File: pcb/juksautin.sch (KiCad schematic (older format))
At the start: 26 parts, among them J1 Screw_Terminal_01x09, J3 AVR-ISP-6, J4 Conn_01x09, U1 SP3485EN, U2 SRV05-4, U3 R-78E5.0-0.5, U4 ATmega328P-AU, Y1 X322516MLB4SI

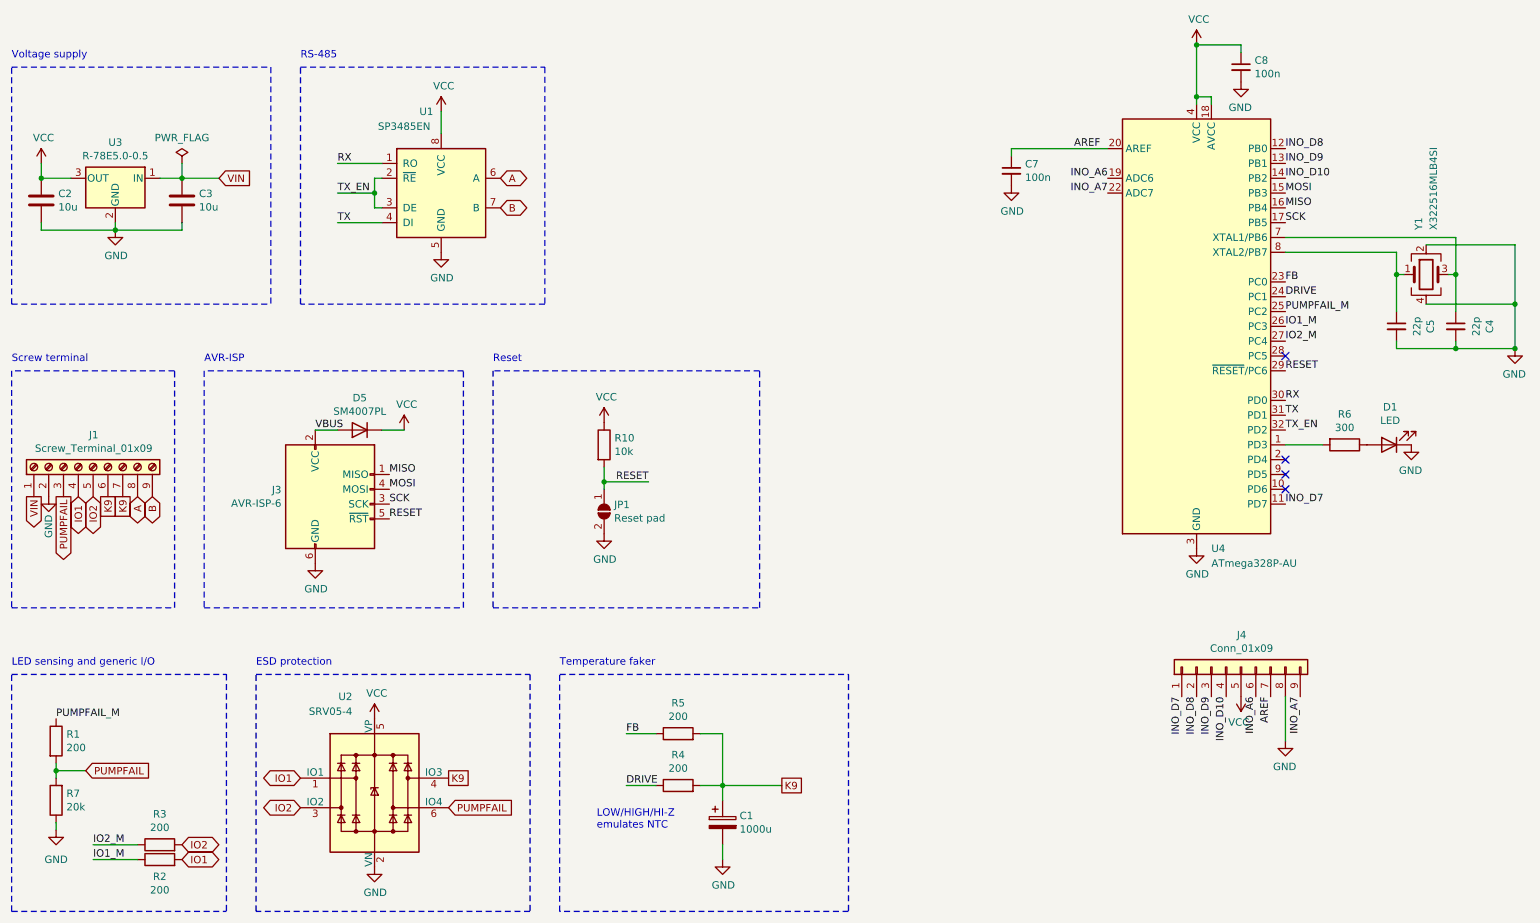
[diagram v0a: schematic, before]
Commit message: pcb: Add debug header for serial comm, reduce unique capacitor count by 1
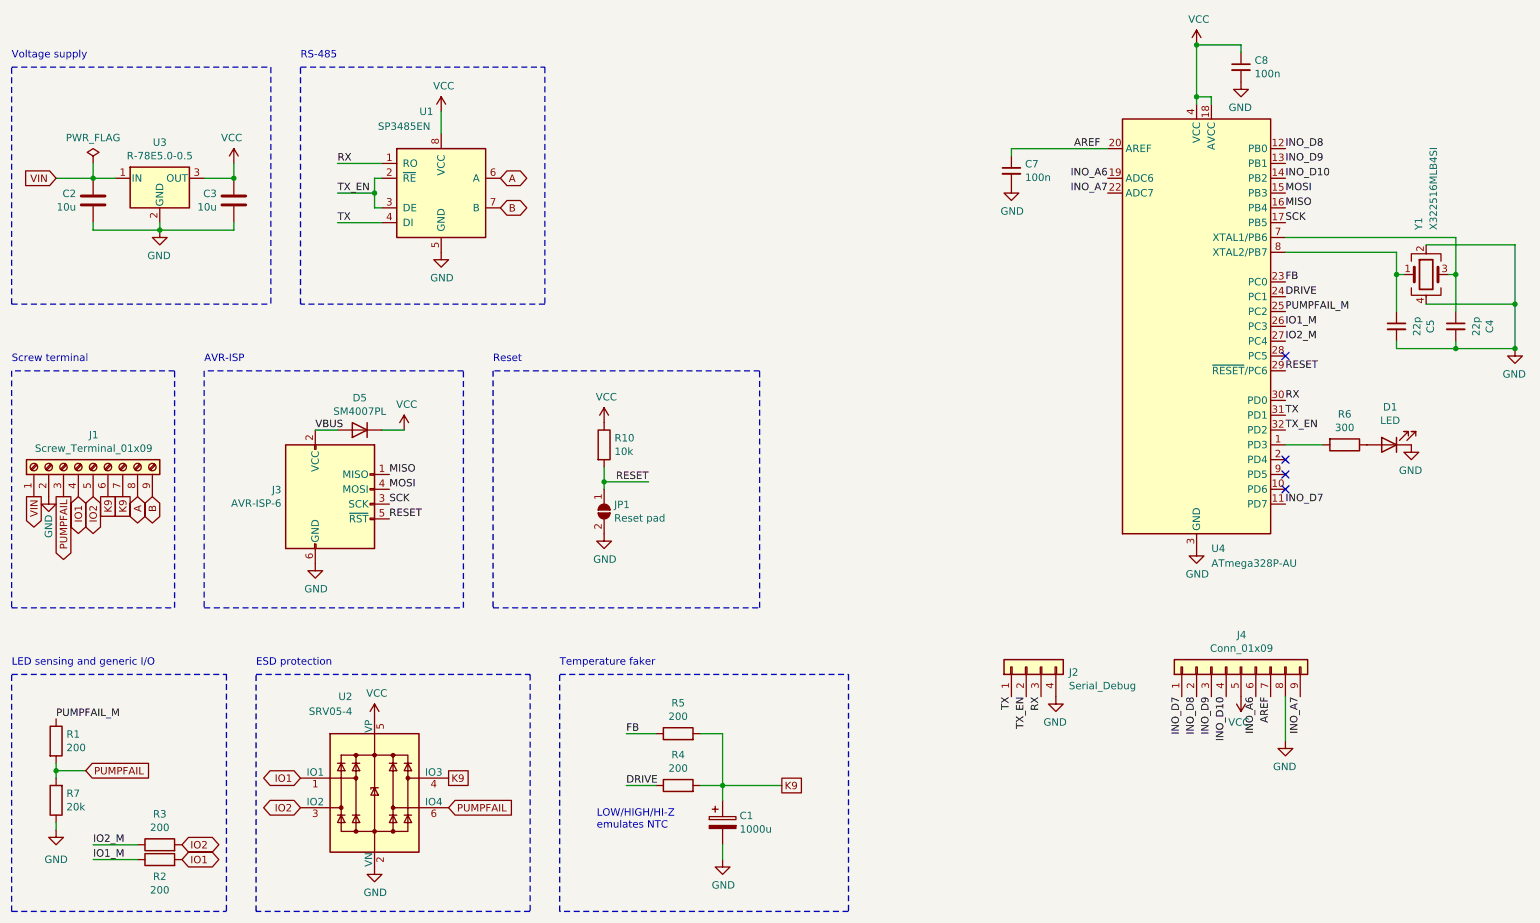
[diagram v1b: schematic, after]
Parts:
- removed C2: 10u, Capacitor_SMD:C_0402_1005Metric, symbol Device:C
- added C3: 10u, Capacitor_SMD:C_1206_3216Metric, symbol Device:C
- added J2: Serial_Debug, Connector_PinHeader_1.27mm:PinHeader_1x04_P1.27mm_Vertical, symbol Connector_Generic:Conn_01x04
- renumbered C3 to C2
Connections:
- net GND: now also C3.2, J2.4 (Pin_4)
- net RX: now also J2.3 (Pin_3)
- net TX: now also J2.1 (Pin_1)
- net TX_EN: now also J2.2 (Pin_2)
- net VCC: now also C3.1
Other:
- moved on the sheet: C2, U3
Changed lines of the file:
@@
 L power:GND #PWR0109
 U 1 1 60C41985
-P 1550 2100
-F 0 "#PWR0109" H 1550 1850 50  0001 C CNN
-F 1 "GND" H 1555 1927 50  0000 C CNN
-F 2 "" H 1550 2100 50  0001 C CNN
-F 3 "" H 1550 2100 50  0001 C CNN
-	1    1550 2100
-	1    0    0    -1
-$EndComp
-Text GLabel 2250 1750 2    50   Input ~ 0
+P 1850 2100
+F 0 "#PWR0109" H 1850 1850 50  0001 C CNN
+F 1 "GND" H 1855 1927 50  0000 C CNN
+F 2 "" H 1850 2100 50  0001 C CNN
+F 3 "" H 1850 2100 50  0001 C CNN
+	1    1850 2100
+	-1   0    0    -1
+$EndComp
+Text GLabel 1150 1750 0    50   Input ~ 0
 VIN
 $Comp
 L power:PWR_FLAG #FLG0101
 U 1 1 60C4198C
-P 2000 1650
-F 0 "#FLG0101" H 2000 1725 50  0001 C CNN
-F 1 "PWR_FLAG" H 2000 1823 50  0000 C CNN
-F 2 "" H 2000 1650 50  0001 C CNN
-F 3 "~" H 2000 1650 50  0001 C CNN
-	1    2000 1650
-	1    0    0    -1
+P 1400 1650
+F 0 "#FLG0101" H 1400 1725 50  0001 C CNN
+F 1 "PWR_FLAG" H 1400 1823 50  0000 C CNN
+F 2 "" H 1400 1650 50  0001 C CNN
+F 3 "~" H 1400 1650 50  0001 C CNN
+	1    1400 1650
+	-1   0    0    -1
 $EndComp
 $Comp
 L Regulator_Switching:R-78E5.0-0.5 U3
 U 1 1 60C41992
-P 1550 1750
-F 0 "U3" H 1550 1992 50  0000 C CNN
-F 1 "R-78E5.0-0.5" H 1550 1901 50  0000 C CNN
-F 2 "Converter_DCDC:Converter_DCDC_RECOM_R-78E-0.5_THT" H 1600 1500 50  0001 L CIN
-F 3 "https://www.recom-power.com/pdf/Innoline/R-78Exx-0.5.pdf" H 1550 1750 50  0001 C CNN
-	1    1550 1750
-	-1   0    0    -1
-$EndComp
-Wire Wire Line
-	1850 1750 2000 1750
-Wire Wire Line
-	2000 1650 2000 1750
-Connection ~ 2000 1750
-Wire Wire Line
-	2000 1750 2250 1750
-Wire Wire Line
-	1550 2050 1550 2100
-Connection ~ 1550 2100
-Wire Wire Line
-	2000 2050 2000 2100
-Wire Wire Line
-	2000 2100 1550 2100
+P 1850 1750
+F 0 "U3" H 1850 1992 50  0000 C CNN
+F 1 "R-78E5.0-0.5" H 1850 1901 50  0000 C CNN
+F 2 "Converter_DCDC:Converter_DCDC_RECOM_R-78E-0.5_THT" H 1900 1500 50  0001 L CIN
+F 3 "https://www.recom-power.com/pdf/Innoline/R-78Exx-0.5.pdf" H 1850 1750 50  0001 C CNN
+	1    1850 1750
+	1    0    0    -1
+$EndComp
+Wire Wire Line
+	1550 1750 1400 1750
+Wire Wire Line
+	1400 1650 1400 1750
+Connection ~ 1400 1750
+Wire Wire Line
+	1400 1750 1150 1750
+Wire Wire Line
+	1850 2050 1850 2100
+Connection ~ 1850 2100
+Wire Wire Line
+	1400 2050 1400 2100
+Wire Wire Line
+	1400 2100 1850 2100
 $Comp
 L power:VCC #PWR0111
 U 1 1 60C419A0
-P 1050 1650
-F 0 "#PWR0111" H 1050 1500 50  0001 C CNN
-F 1 "VCC" H 1065 1823 50  0000 C CNN
-F 2 "" H 1050 1650 50  0001 C CNN
-F 3 "" H 1050 1650 50  0001 C CNN
-	1    1050 1650
-	1    0    0    -1
-$EndComp
-Wire Wire Line
-	1250 1750 1050 1750
+P 2350 1650
+F 0 "#PWR0111" H 2350 1500 50  0001 C CNN
+F 1 "VCC" H 2365 1823 50  0000 C CNN
+F 2 "" H 2350 1650 50  0001 C CNN
+F 3 "" H 2350 1650 50  0001 C CNN
+	1    2350 1650
+	-1   0    0    -1
+$EndComp
+Wire Wire Line
+	2150 1750 2350 1750
 Wire Notes Line
 	850  1000 2600 1000
@@
 Text Notes 850  950  0    50   ~ 0
 Voltage supply
-$Comp
-L Device:C C2
-U 1 1 60C419AC
-P 1050 1900
-F 0 "C2" H 1165 1946 50  0000 L CNN
-F 1 "10u" H 1165 1855 50  0000 L CNN
-F 2 "Capacitor_SMD:C_0402_1005Metric" H 1088 1750 50  0001 C CNN
-F 3 "~" H 1050 1900 50  0001 C CNN
-F 4 "C15525" H 1050 1900 50  0001 C CNN "LCSC"
-	1    1050 1900
-	1    0    0    -1
-$EndComp
-$Comp
-L Device:C C3
-U 1 1 60C419B2
-P 2000 1900
-F 0 "C3" H 2115 1946 50  0000 L CNN
-F 1 "10u" H 2115 1855 50  0000 L CNN
-F 2 "Capacitor_SMD:C_1206_3216Metric" H 2038 1750 50  0001 C CNN
-F 3 "~" H 2000 1900 50  0001 C CNN
-F 4 "C13585" H 2000 1900 50  0001 C CNN "LCSC"
-	1    2000 1900
-	1    0    0    -1
-$EndComp
-Connection ~ 1050 1750
-Wire Wire Line
-	1550 2100 1050 2100
-Wire Wire Line
-	1050 2100 1050 2050
-Wire Wire Line
-	1050 1650 1050 1750
+Wire Wire Line
+	1850 2100 2350 2100
+Wire Wire Line
+	2350 2100 2350 2050
+Wire Wire Line
+	2350 1650 2350 1750
 Wire Notes Line
 	850  2600 2600 2600
@@
 Wire Wire Line
 	10600 2900 10200 2900
+Text Label 7800 5250 3    50   ~ 0
+RX
+Text Label 7600 5250 3    50   ~ 0
+TX
+Text Label 7700 5250 3    50   ~ 0
+TX_EN
+$Comp
+L power:GND #PWR0110
+U 1 1 60D1EC45
+P 7900 5250
+F 0 "#PWR0110" H 7900 5000 50  0001 C CNN
+F 1 "GND" H 7905 5077 50  0000 C CNN
+F 2 "" H 7900 5250 50  0001 C CNN
+F 3 "" H 7900 5250 50  0001 C CNN
+	1    7900 5250
+	-1   0    0    -1
+$EndComp
+$Comp
+L Connector_Generic:Conn_01x04 J2
+U 1 1 60D1A962
+P 7700 5050
+F 0 "J2" V 7664 4762 50  0000 R CNN
+F 1 "Serial_Debug" V 7573 4762 50  0000 R CNN
+F 2 "Connector_PinHeader_1.27mm:PinHeader_1x04_P1.27mm_Vertical" H 7700 5050 50  0001 C CNN
+F 3 "~" H 7700 5050 50  0001 C CNN
+	1    7700 5050
+	0    -1   -1   0
+$EndComp
+$Comp
+L Device:C C2
+U 1 1 60C419B2
+P 1400 1900
+F 0 "C2" H 1515 1946 50  0000 L CNN
+F 1 "10u" H 1515 1855 50  0000 L CNN
+F 2 "Capacitor_SMD:C_1206_3216Metric" H 1438 1750 50  0001 C CNN
+F 3 "~" H 1400 1900 50  0001 C CNN
+F 4 "C13585" H 1400 1900 50  0001 C CNN "LCSC"
+	1    1400 1900
+	-1   0    0    -1
+$EndComp
+$Comp
+L Device:C C3
+U 1 1 60D40841
+P 2350 1900
+F 0 "C3" H 2465 1946 50  0000 L CNN
+F 1 "10u" H 2465 1855 50  0000 L CNN
+F 2 "Capacitor_SMD:C_1206_3216Metric" H 2388 1750 50  0001 C CNN
+F 3 "~" H 2350 1900 50  0001 C CNN
+F 4 "C13585" H 2350 1900 50  0001 C CNN "LCSC"
+	1    2350 1900
+	-1   0    0    -1
+$EndComp
+Connection ~ 2350 1750
 $EndSCHEMATC

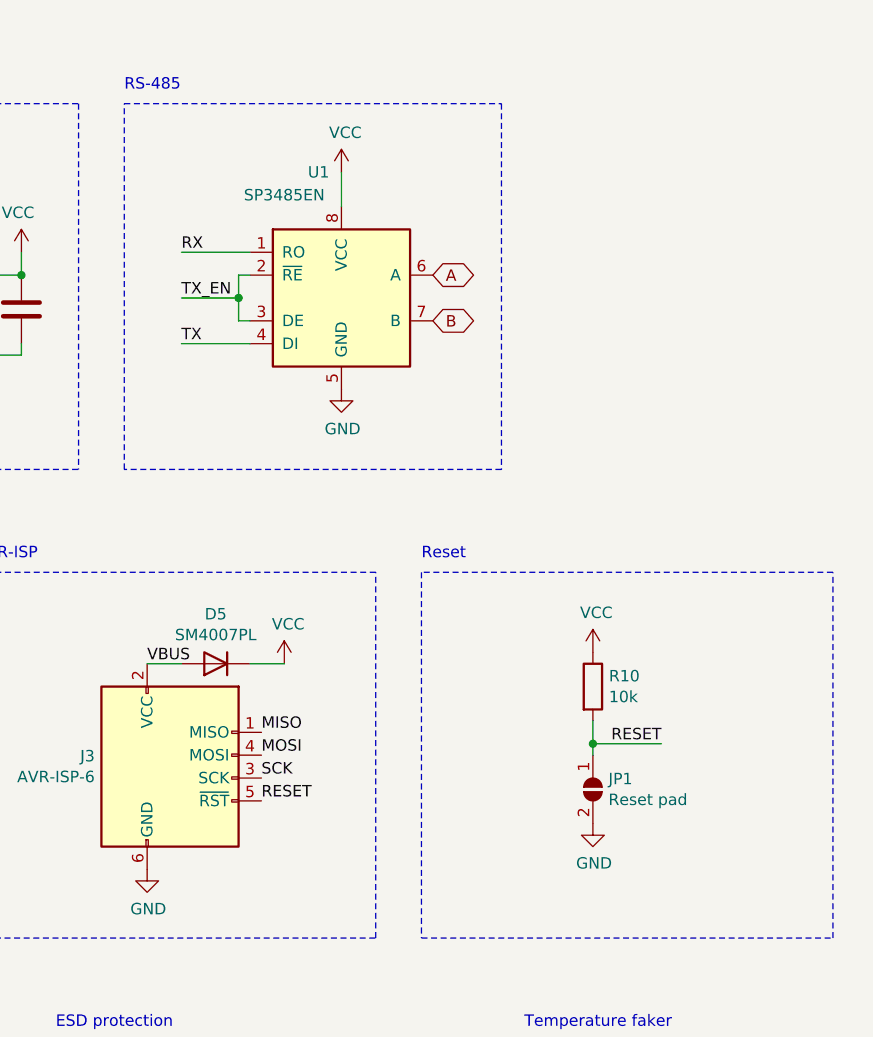
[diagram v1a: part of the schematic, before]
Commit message: pcb: Remove reset pad (we have header anyway) and and RX pull-up
RX pull-up seems to be required to keep RX HIGH during transmit phase
when SP3485 is HI-Z.
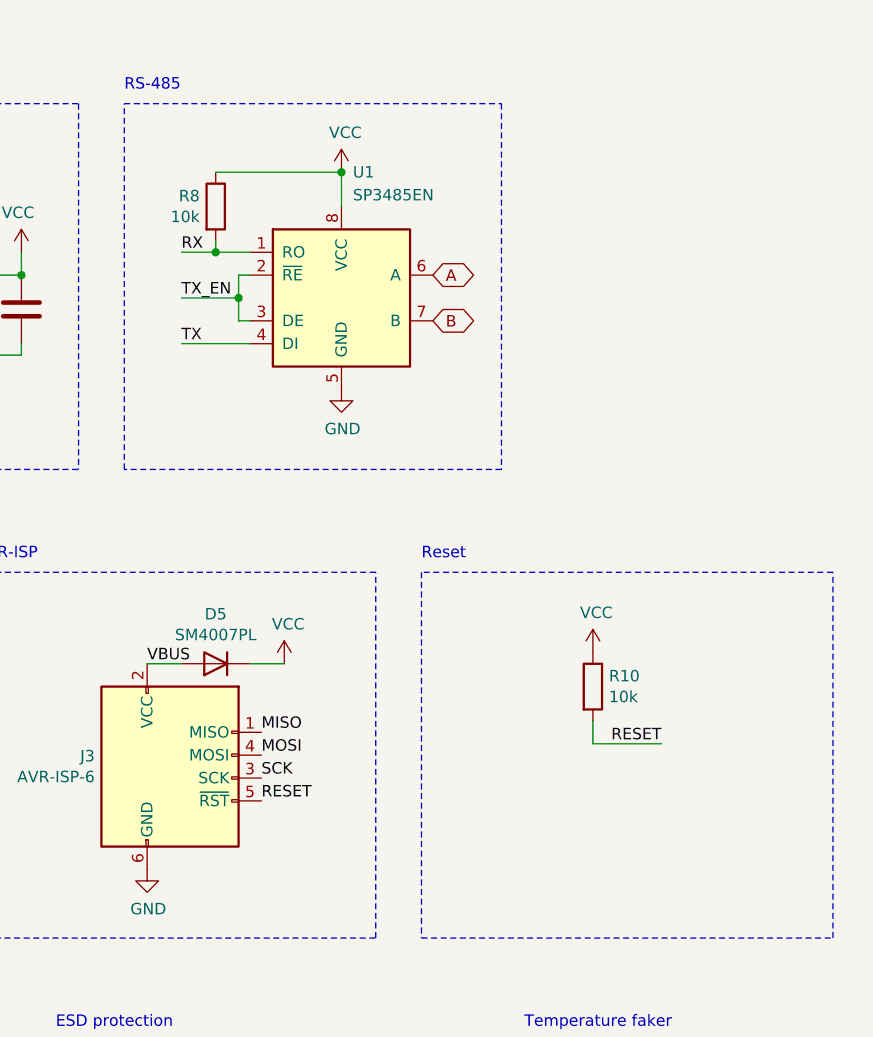
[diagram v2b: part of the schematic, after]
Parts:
- removed JP1: Reset pad, Jumper:SolderJumper-2_P1.3mm_Open_Pad1.0x1.5mm, symbol Jumper:SolderJumper_2_Open
- added R8: 10k, Resistor_SMD:R_0603_1608Metric, symbol Device:R
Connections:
- net RX: now also R8.2
- net VCC: now also R8.1
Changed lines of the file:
@@
 U 1 1 60BB9B57
 P 3750 1850
-F 0 "U1" H 3650 2400 50  0000 C CNN
-F 1 "SP3485EN" H 3500 2300 50  0000 C CNN
+F 0 "U1" H 3800 2400 50  0000 L CNN
+F 1 "SP3485EN" H 3800 2300 50  0000 L CNN
 F 2 "Package_SO:SOIC-8_3.9x4.9mm_P1.27mm" H 4800 1500 50  0001 C CIN
 F 3 "http://www.icbase.com/pdf/SPX/SPX00480106.pdf" H 3750 1850 50  0001 C CNN
@@
 RX
 Wire Wire Line
-	3050 1650 3350 1650
+	3050 1650 3200 1650
 Text Label 3050 2050 0    50   ~ 0
 TX
@@
 Text Label 9450 3050 0    50   ~ 0
 RESET
-$Comp
-L power:GND #PWR0102
-U 1 1 60EDAA2A
-P 4850 4150
-F 0 "#PWR0102" H 4850 3900 50  0001 C CNN
-F 1 "GND" H 4855 3977 50  0000 C CNN
-F 2 "" H 4850 4150 50  0001 C CNN
-F 3 "" H 4850 4150 50  0001 C CNN
-	1    4850 4150
-	1    0    0    -1
-$EndComp
-$Comp
-L Jumper:SolderJumper_2_Open JP1
-U 1 1 60EE7989
-P 4850 4000
-F 0 "JP1" V 4804 4068 50  0000 L CNN
-F 1 "Reset pad" V 4895 4068 50  0000 L CNN
-F 2 "Jumper:SolderJumper-2_P1.3mm_Open_Pad1.0x1.5mm" H 4850 4000 50  0001 C CNN
-F 3 "~" H 4850 4000 50  0001 C CNN
-	1    4850 4000
-	0    1    1    0
-$EndComp
 Wire Wire Line
 	7600 1550 8250 1550
@@
 	9150 850  8850 850
 Connection ~ 8850 850
-Connection ~ 4850 3800
 Text Label 5150 3800 2    50   ~ 0
 RESET
@@
 Text Label 3400 4050 0    50   ~ 0
 RESET
-Wire Wire Line
-	4850 3850 4850 3800
 NoConn ~ 9450 3650
 NoConn ~ 9450 3750
@@
 $EndComp
 Connection ~ 2350 1750
+$Comp
+L Device:R R8
+U 1 1 60D023E7
+P 3200 1450
+F 0 "R8" H 3130 1496 50  0000 R CNN
+F 1 "10k" H 3130 1405 50  0000 R CNN
+F 2 "Resistor_SMD:R_0603_1608Metric" V 3130 1450 50  0001 C CNN
+F 3 "~" H 3200 1450 50  0001 C CNN
+F 4 "C25804" H 3200 1450 50  0001 C CNN "LCSC"
+	1    3200 1450
+	1    0    0    -1
+$EndComp
+Wire Wire Line
+	3200 1600 3200 1650
+Connection ~ 3200 1650
+Wire Wire Line
+	3200 1650 3350 1650
+Wire Wire Line
+	3200 1300 3750 1300
+Connection ~ 3750 1300
 $EndSCHEMATC

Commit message: pcb: Some changes. Don't remember anymore.
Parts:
- R8: value 10k -> 20k; LCSC C25804 -> C4184
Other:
- moved on the sheet: R8, U1
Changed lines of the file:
@@
 L power:GND #PWR0101
 U 1 1 60C357A5
-P 3750 2250
-F 0 "#PWR0101" H 3750 2000 50  0001 C CNN
-F 1 "GND" H 3755 2077 50  0000 C CNN
-F 2 "" H 3750 2250 50  0001 C CNN
-F 3 "" H 3750 2250 50  0001 C CNN
-	1    3750 2250
+P 3750 2300
+F 0 "#PWR0101" H 3750 2050 50  0001 C CNN
+F 1 "GND" H 3755 2127 50  0000 C CNN
+F 2 "" H 3750 2300 50  0001 C CNN
+F 3 "" H 3750 2300 50  0001 C CNN
+	1    3750 2300
 	1    0    0    -1
 $EndComp
@@
 LOW/HIGH/HI-Z\nemulates NTC
 Wire Wire Line
-	3350 1950 3300 1950
-Wire Wire Line
-	3350 1750 3300 1750
-Wire Wire Line
-	3300 1750 3300 1850
+	3350 2000 3300 2000
+Wire Wire Line
+	3350 1800 3300 1800
+Wire Wire Line
+	3300 1800 3300 1900
 Wire Wire Line
 	5650 5850 5650 5950
@@
 $EndComp
 Wire Wire Line
-	3750 1450 3750 1300
+	3750 1500 3750 1350
 $Comp
 L power:VCC #PWR0107
@@
 Text GLabel 1500 3900 3    50   UnSpc ~ 0
 K9
-Text GLabel 4150 1750 2    50   3State ~ 0
+Text GLabel 4150 1800 2    50   3State ~ 0
 A
-Text GLabel 4150 1950 2    50   3State ~ 0
+Text GLabel 4150 2000 2    50   3State ~ 0
 B
 Wire Wire Line
@@
 Text Notes 850  3000 0    50   ~ 0
 Screw terminal
-Connection ~ 3300 1850
-Wire Wire Line
-	3300 1850 3300 1950
+Connection ~ 3300 1900
+Wire Wire Line
+	3300 1900 3300 2000
 Wire Notes Line
 	2800 1000 4450 1000
@@
 L Interface_UART:SP3485EN U1
 U 1 1 60BB9B57
-P 3750 1850
+P 3750 1900
 F 0 "U1" H 3800 2400 50  0000 L CNN
 F 1 "SP3485EN" H 3800 2300 50  0000 L CNN
-F 2 "Package_SO:SOIC-8_3.9x4.9mm_P1.27mm" H 4800 1500 50  0001 C CIN
-F 3 "http://www.icbase.com/pdf/SPX/SPX00480106.pdf" H 3750 1850 50  0001 C CNN
-F 4 "C8963" H 3750 1850 50  0001 C CNN "LCSC"
-	1    3750 1850
+F 2 "Package_SO:SOIC-8_3.9x4.9mm_P1.27mm" H 4800 1550 50  0001 C CIN
+F 3 "http://www.icbase.com/pdf/SPX/SPX00480106.pdf" H 3750 1900 50  0001 C CNN
+F 4 "C8963" H 3750 1900 50  0001 C CNN "LCSC"
+	1    3750 1900
 	1    0    0    -1
 $EndComp
@@
 	1    0    0    -1
 $EndComp
-Text Label 3050 1650 0    50   ~ 0
+Text Label 3050 1700 0    50   ~ 0
 RX
 Wire Wire Line
-	3050 1650 3200 1650
-Text Label 3050 2050 0    50   ~ 0
+	3050 1700 3200 1700
+Text Label 3050 2100 0    50   ~ 0
 TX
 Wire Wire Line
-	3050 2050 3350 2050
+	3050 2100 3350 2100
 Text Label 9450 3250 0    50   ~ 0
 RX
@@
 Text Label 9450 3450 0    50   ~ 0
 TX_EN
-Text Label 3050 1850 0    50   ~ 0
+Text Label 3050 1900 0    50   ~ 0
 TX_EN
 Wire Wire Line
-	3050 1850 3300 1850
+	3050 1900 3300 1900
 Text Label 1150 5400 0    50   ~ 0
 PUMPFAIL_M
@@
 L Device:R R8
 U 1 1 60D023E7
-P 3200 1450
-F 0 "R8" H 3130 1496 50  0000 R CNN
-F 1 "10k" H 3130 1405 50  0000 R CNN
-F 2 "Resistor_SMD:R_0603_1608Metric" V 3130 1450 50  0001 C CNN
-F 3 "~" H 3200 1450 50  0001 C CNN
-F 4 "C25804" H 3200 1450 50  0001 C CNN "LCSC"
-	1    3200 1450
-	1    0    0    -1
-$EndComp
-Wire Wire Line
-	3200 1600 3200 1650
-Connection ~ 3200 1650
-Wire Wire Line
-	3200 1650 3350 1650
-Wire Wire Line
-	3200 1300 3750 1300
-Connection ~ 3750 1300
+P 3200 1500
+F 0 "R8" H 3130 1546 50  0000 R CNN
+F 1 "20k" H 3130 1455 50  0000 R CNN
+F 2 "Resistor_SMD:R_0603_1608Metric" V 3130 1500 50  0001 C CNN
+F 3 "~" H 3200 1500 50  0001 C CNN
+F 4 "C4184" H 3200 1500 50  0001 C CNN "LCSC"
+	1    3200 1500
+	1    0    0    -1
+$EndComp
+Wire Wire Line
+	3200 1650 3200 1700
+Connection ~ 3200 1700
+Wire Wire Line
+	3200 1700 3350 1700
+Wire Wire Line
+	3200 1350 3750 1350
+Connection ~ 3750 1350
+Wire Wire Line
+	3750 1300 3750 1350
 $EndSCHEMATC
